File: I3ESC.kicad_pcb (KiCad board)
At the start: 4 copper layers, 64 x 54 mm, 153 parts, among them J1 JST SR/SZ, J10 VIN_BARREL, J11 Barrel_Jack, J12 JST SR/SZ, J13 Conn_SWD, J2 Screw_Terminal_01x02, J3 Screw_Terminal_01x02, J4 Screw_Terminal_01x02, J5 Encoder1, J7 VIN_TERMINAL, J8 Encoder2, J9 JST SR/SZ, SW2 boot-red, SW3 user1-white, U1 SY8113BADC, U10 USBLC6-2P6, U12 FD8288T (DRV8300), U2 FD8288T (DRV8300), U3 SPX3819M5-L-3-3, U4 STM32G474RETx, U5 Qwiic1, U7 Qwiic2, U8 ABM3B-8.000MHZ, U9 USB_C_Receptacle

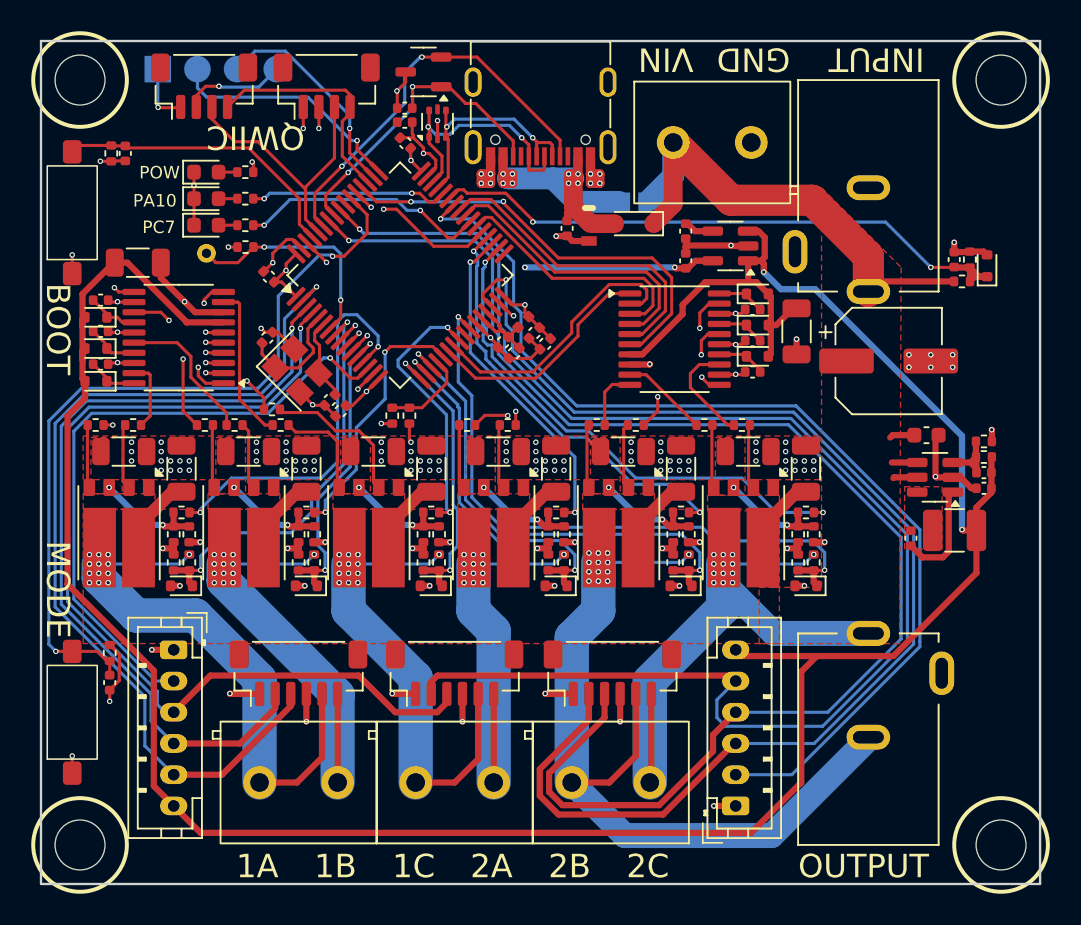
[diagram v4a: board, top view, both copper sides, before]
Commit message: Add decoupling capacitor to PG10 and update footprints
Added C17 (100nF, 50V) capacitor to PG10 for improved decoupling. Updated several footprint and property fields, fixed layer and sheetname attributes, and made minor net and pad stack changes for consistency with KiCAD 9.0. Updated LCSC part number for JST SH connector.
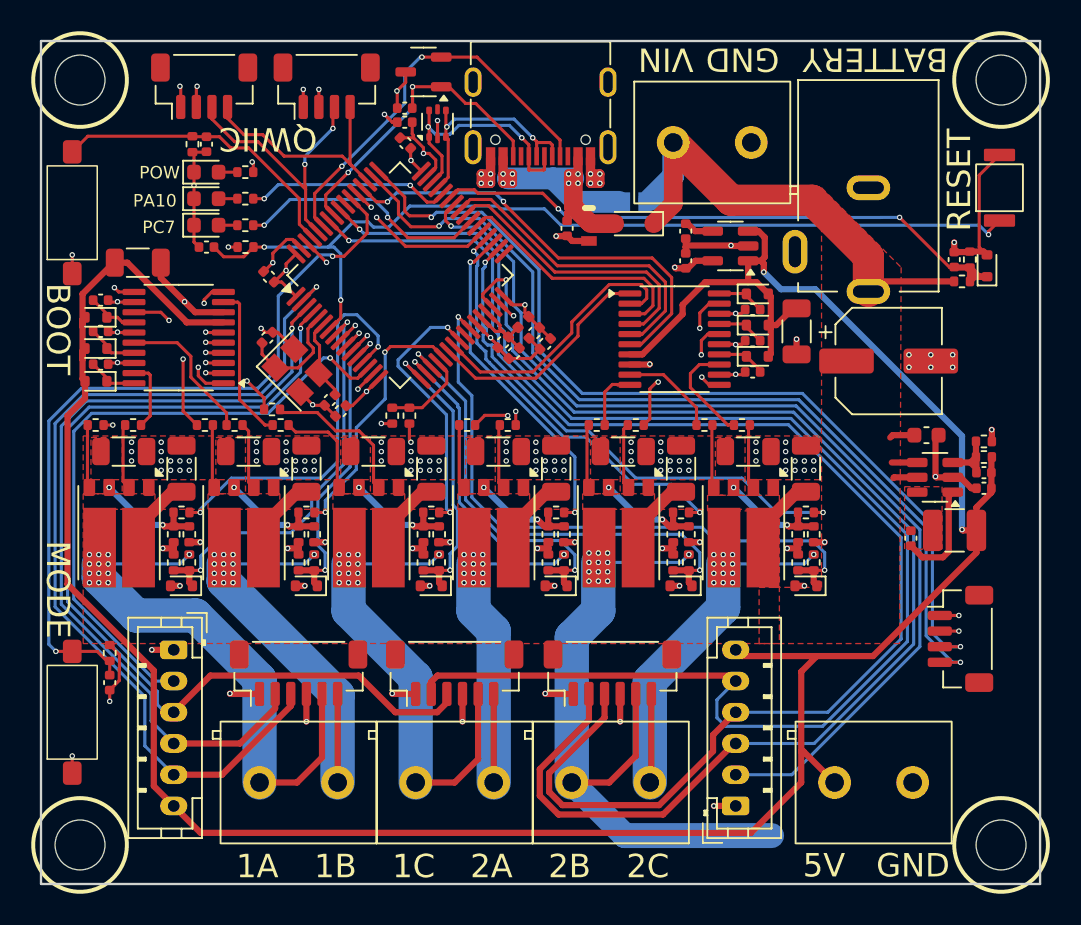
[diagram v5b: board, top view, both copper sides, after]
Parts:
- removed J11: Barrel_Jack, AlfredoFootprints:DC-005C_1
- removed J13: Conn_SWD, Connector_PinHeader_2.54mm:PinHeader_1x04_P2.54mm_Vertical
- removed TP3: RST, AlfredoFootprints:GE_TestPoint_Loop
- added C17: 100nF, 50V, Capacitor_SMD:C_0402_1005Metric, F.Cu at (-21.4, -13.8)
- added J6: 5V out, AlfredoFootprints:TerminalBlock_Ningbo_2P_5mm, F.Cu at (21.3, 20.5)
- added SW1: reset, AlfredoFootprints:Button_SKRKAEE020, F.Cu at (29.4, -17.6)
- added U11: Qwiic2, Connector_JST:JST_SH_BM04B-SRSS-TB_1x04-1MP_P1.00mm_Vertical, F.Cu at (-13.7, -24.1)
- D84: value LED_Green -> LED_Yellow
- U7: value Qwiic2 -> Prog
- moved U7 53.9 mm to (26.9, 11.3), turned to -90 degrees
- moved C23 5.23 mm to (-21.4, -20.4)
- moved R2 5.23 mm to (-22.3, -20.4)
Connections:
- U7 pad 3: SDA -> SWDIO
- U7 pad 4: SCL -> SWCLK
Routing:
- net SWCLK: track 13.9 -> 59.8 mm, vias 1 -> 2
- net Net-(U4-PG10): track 14.6 -> 59.6 mm, vias 2 -> 3
- net SWDIO: track 15.4 -> 59.2 mm, vias 1 -> 2
- net /IE-PHASES/IE-FETS-2C/SHx: track 51.4 -> 40.7 mm
- net /IE-PHASES/IE-FETS-2B/SHx: track 72.2 -> 63.4 mm
- net GND: track 95.2 -> 102.9 mm
- net +3V3: track 164.8 -> 169.4 mm
- net +5V: track 173.2 -> 175.4 mm
- net CC1: track 26.1 -> 27.6 mm, vias 2 -> 3
- net IN_H_1A: track 29.4 -> 30.2 mm
- net /IE-PHASES/IE-FETS-2C/GLx: track 5.60 -> 6.25 mm
- net SDA: track 18.3 -> 18.4 mm, vias 0 -> 2
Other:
- board text added: "5V"
- board text added: "BATTERY"
- board text added: "RESET"
- board text removed: "3V3"
- board text removed: "INPUT"
- board text removed: "OUTPUT"
- board text removed: "SCL"
- board text removed: "SDA"
